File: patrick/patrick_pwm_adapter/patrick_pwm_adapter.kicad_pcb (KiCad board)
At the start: 2 copper layers, 5 parts, among them J1 Conn_01x13, J2 Conn_01x14, U1 TLC5951DAP

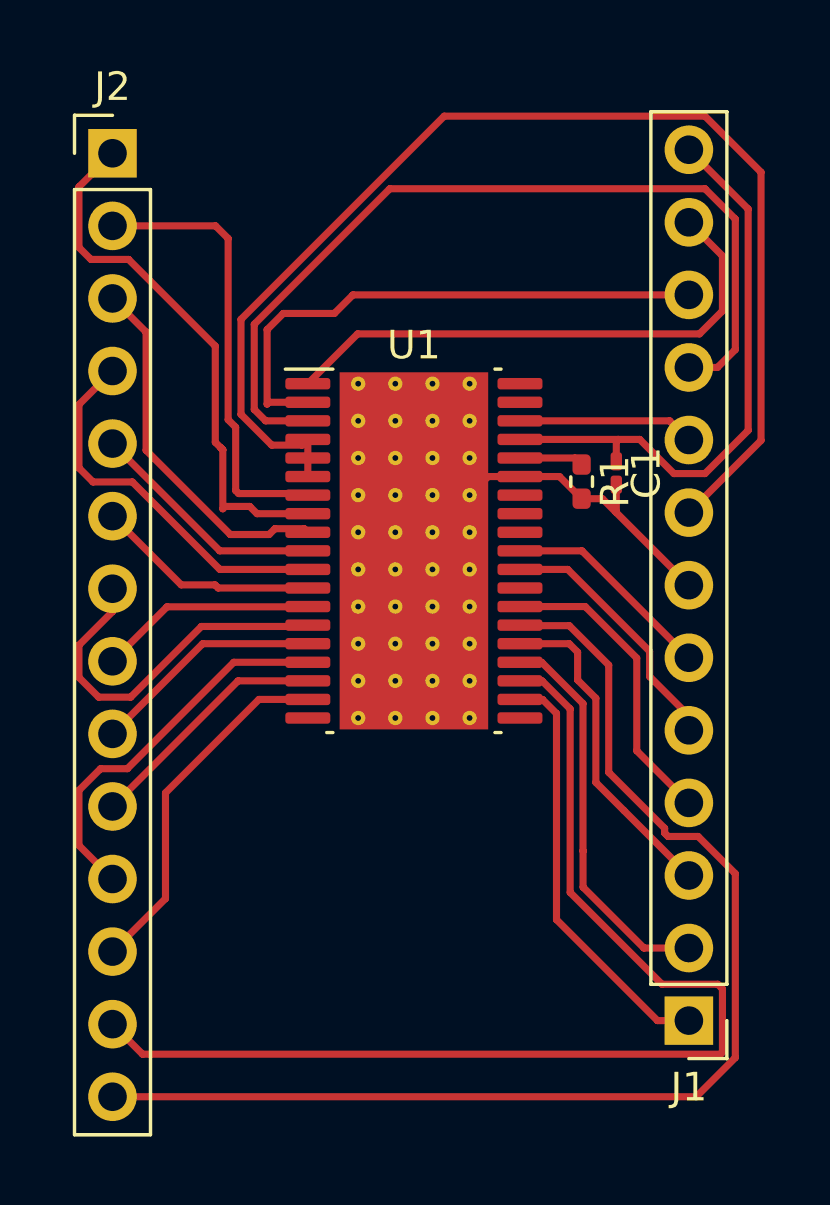
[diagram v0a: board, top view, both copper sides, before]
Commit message: added pwm breakouts
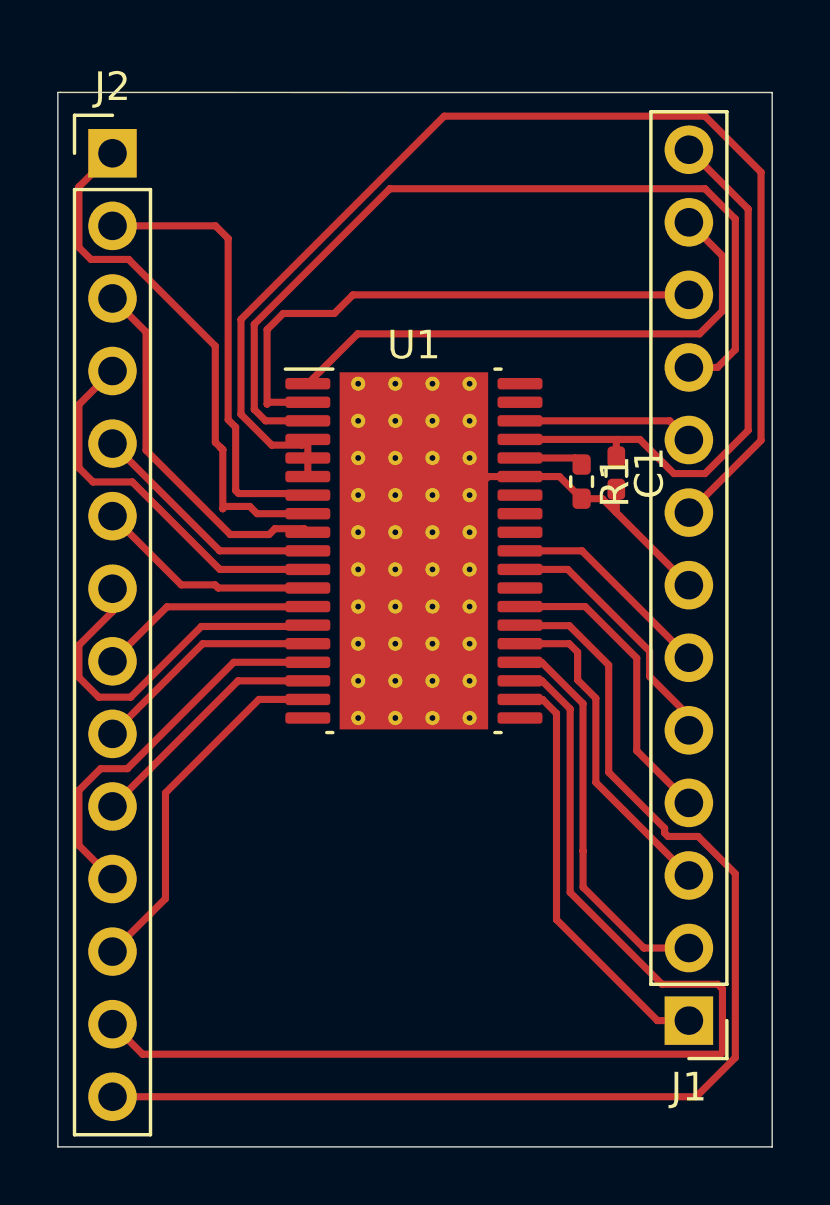
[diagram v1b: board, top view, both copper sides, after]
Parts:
- C1: footprint Capacitor_SMD:C_0201_0603Metric_Pad0.64x0.40mm_HandSolder -> Capacitor_SMD:C_0402_1005Metric_Pad0.74x0.62mm_HandSolder
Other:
- board outline added: 25 x 36.9 mm
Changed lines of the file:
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@@
   (general
     (thickness 1.6)
-    (drawings 0)
+    (drawings 5)
     (tracks 173)
     (zones 0)
@@
     (add_net "Net-(U1-Pad38)")
   )
+  (module Capacitor_SMD:C_0402_1005Metric_Pad0.74x0.62mm_HandSolder (layer F.Cu)
+    (at 166.05758 51.2456 270)
+    (descr "Capacitor SMD 0402 (1005 Metric), square (rectangular) end terminal, IPC_7351 nominal with elongated pad for handsoldering. (Body size source: IPC-SM-782 page 76, https://www.pcb-3d.com/wordpress/wp-content/uploads/ipc-sm-782a_amendment_1_and_2.pdf), generated with kicad-footprint-generator")
+    (tags "capacitor handsolder")
+    (attr smd)
+    (fp_text reference C1 (at 0 -1.16 90) (layer F.SilkS)
+      (effects (font (size 1 1) (thickness 0.15)))
+    )
+    (fp_text value C (at 0 1.16 90) (layer F.Fab)
+      (effects (font (size 1 1) (thickness 0.15)))
+    )
+    (fp_line (start 1.08 0.46) (end -1.08 0.46) (layer F.CrtYd) (width 0.05))
+    (fp_line (start 1.08 -0.46) (end 1.08 0.46) (layer F.CrtYd) (width 0.05))
+    (fp_line (start -1.08 -0.46) (end 1.08 -0.46) (layer F.CrtYd) (width 0.05))
+    (fp_line (start -1.08 0.46) (end -1.08 -0.46) (layer F.CrtYd) (width 0.05))
+    (fp_line (start -0.115835 0.36) (end 0.115835 0.36) (layer F.SilkS) (width 0.12))
+    (fp_line (start -0.115835 -0.36) (end 0.115835 -0.36) (layer F.SilkS) (width 0.12))
+    (fp_line (start 0.5 0.25) (end -0.5 0.25) (layer F.Fab) (width 0.1))
+    (fp_line (start 0.5 -0.25) (end 0.5 0.25) (layer F.Fab) (width 0.1))
+    (fp_line (start -0.5 -0.25) (end 0.5 -0.25) (layer F.Fab) (width 0.1))
+    (fp_line (start -0.5 0.25) (end -0.5 -0.25) (layer F.Fab) (width 0.1))
+    (fp_text user %R (at 0 0 90) (layer F.Fab)
+      (effects (font (size 0.25 0.25) (thickness 0.04)))
+    )
+    (pad 2 smd roundrect (at 0.5675 0 270) (size 0.735 0.62) (layers F.Cu F.Paste F.Mask) (roundrect_rratio 0.25)
+      (net 10 /GND))
+    (pad 1 smd roundrect (at -0.5675 0 270) (size 0.735 0.62) (layers F.Cu F.Paste F.Mask) (roundrect_rratio 0.25)
+      (net 11 /VCC))
+    (model ${KISYS3DMOD}/Capacitor_SMD.3dshapes/C_0402_1005Metric.wrl
+      (at (xyz 0 0 0))
+      (scale (xyz 1 1 1))
+      (rotate (xyz 0 0 0))
+    )
+  )
   (module Resistor_SMD:R_0402_1005Metric_Pad0.72x0.64mm_HandSolder (layer F.Cu)
     (at 164.84346 51.54736 270)
@@
     (fp_text value R_Small_US (at 0 1.17 90) (layer F.Fab)
       (effects (font (size 1 1) (thickness 0.15)))
-    )
-    (fp_text user %R (at 0 0 90) (layer F.Fab)
-      (effects (font (size 0.26 0.26) (thickness 0.04)))
     )
     (fp_line (start -0.525 0.27) (end -0.525 -0.27) (layer F.Fab) (width 0.1))
@@
     (fp_line (start 1.1 -0.47) (end 1.1 0.47) (layer F.CrtYd) (width 0.05))
     (fp_line (start 1.1 0.47) (end -1.1 0.47) (layer F.CrtYd) (width 0.05))
+    (fp_text user %R (at 0 0 90) (layer F.Fab)
+      (effects (font (size 0.26 0.26) (thickness 0.04)))
+    )
     (pad 2 smd roundrect (at 0.5975 0 270) (size 0.715 0.64) (layers F.Cu F.Paste F.Mask) (roundrect_rratio 0.25)
       (net 10 /GND))
@@
     )
     (fp_text value TLC5951DAP (at 0 7.2) (layer F.Fab)
-      (effects (font (size 1 1) (thickness 0.15)))
-    )
-    (fp_text user %R (at 0 0) (layer F.Fab)
       (effects (font (size 1 1) (thickness 0.15)))
     )
@@
     (fp_line (start 4.75 6.5) (end 4.75 -6.5) (layer F.CrtYd) (width 0.05))
     (fp_line (start 4.75 -6.5) (end -4.75 -6.5) (layer F.CrtYd) (width 0.05))
+    (fp_text user %R (at 0 0) (layer F.Fab)
+      (effects (font (size 1 1) (thickness 0.15)))
+    )
     (pad "" smd roundrect (at 0.85 2.12) (size 1.37 1.71) (layers F.Paste) (roundrect_rratio 0.182482))
     (pad "" smd roundrect (at 0.85 0) (size 1.37 1.71) (layers F.Paste) (roundrect_rratio 0.182482))
@@
       (effects (font (size 1 1) (thickness 0.15)))
     )
-    (fp_text user %R (at 0 16.51 90) (layer F.Fab)
-      (effects (font (size 1 1) (thickness 0.15)))
-    )
     (fp_line (start -0.635 -1.27) (end 1.27 -1.27) (layer F.Fab) (width 0.1))
     (fp_line (start 1.27 -1.27) (end 1.27 34.29) (layer F.Fab) (width 0.1))
@@
     (fp_line (start 1.8 34.8) (end 1.8 -1.8) (layer F.CrtYd) (width 0.05))
     (fp_line (start 1.8 -1.8) (end -1.8 -1.8) (layer F.CrtYd) (width 0.05))
+    (fp_text user %R (at 0 16.51 90) (layer F.Fab)
+      (effects (font (size 1 1) (thickness 0.15)))
+    )
     (pad 14 thru_hole oval (at 0 33.02) (size 1.7 1.7) (drill 1) (layers *.Cu *.Mask)
       (net 21 /OUT16))
@@
       (effects (font (size 1 1) (thickness 0.15)))
     )
-    (fp_text user %R (at 0 15.24 90) (layer F.Fab)
-      (effects (font (size 1 1) (thickness 0.15)))
-    )
     (fp_line (start -0.635 -1.27) (end 1.27 -1.27) (layer F.Fab) (width 0.1))
     (fp_line (start 1.27 -1.27) (end 1.27 31.75) (layer F.Fab) (width 0.1))
@@
     (fp_line (start 1.8 32.25) (end 1.8 -1.8) (layer F.CrtYd) (width 0.05))
     (fp_line (start 1.8 -1.8) (end -1.8 -1.8) (layer F.CrtYd) (width 0.05))
+    (fp_text user %R (at 0 15.24 90) (layer F.Fab)
+      (effects (font (size 1 1) (thickness 0.15)))
+    )
     (pad 13 thru_hole oval (at 0 30.48 180) (size 1.7 1.7) (drill 1) (layers *.Cu *.Mask)
       (net 11 /VCC))
@@
     )
   )
-  (module Capacitor_SMD:C_0201_0603Metric_Pad0.64x0.40mm_HandSolder (layer F.Cu)
-    (at 166.05758 51.2456 270)
-    (descr "Capacitor SMD 0201 (0603 Metric), square (rectangular) end terminal, IPC_7351 nominal with elongated pad for handsoldering. (Body size source: https://www.vishay.com/docs/20052/crcw0201e3.pdf), generated with kicad-footprint-generator")
-    (tags "capacitor handsolder")
-    (attr smd)
-    (fp_text reference C1 (at 0 -1.05 90) (layer F.SilkS)
-      (effects (font (size 1 1) (thickness 0.15)))
-    )
-    (fp_text value C (at 0 1.05 90) (layer F.Fab)
-      (effects (font (size 1 1) (thickness 0.15)))
-    )
-    (fp_text user %R (at 0 -0.68 90) (layer F.Fab)
-      (effects (font (size 0.25 0.25) (thickness 0.04)))
-    )
-    (fp_line (start -0.3 0.15) (end -0.3 -0.15) (layer F.Fab) (width 0.1))
-    (fp_line (start -0.3 -0.15) (end 0.3 -0.15) (layer F.Fab) (width 0.1))
-    (fp_line (start 0.3 -0.15) (end 0.3 0.15) (layer F.Fab) (width 0.1))
-    (fp_line (start 0.3 0.15) (end -0.3 0.15) (layer F.Fab) (width 0.1))
-    (fp_line (start -0.88 0.35) (end -0.88 -0.35) (layer F.CrtYd) (width 0.05))
-    (fp_line (start -0.88 -0.35) (end 0.88 -0.35) (layer F.CrtYd) (width 0.05))
-    (fp_line (start 0.88 -0.35) (end 0.88 0.35) (layer F.CrtYd) (width 0.05))
-    (fp_line (start 0.88 0.35) (end -0.88 0.35) (layer F.CrtYd) (width 0.05))
-    (pad 2 smd roundrect (at 0.4075 0 270) (size 0.635 0.4) (layers F.Cu F.Mask) (roundrect_rratio 0.25)
-      (net 10 /GND))
-    (pad 1 smd roundrect (at -0.4075 0 270) (size 0.635 0.4) (layers F.Cu F.Mask) (roundrect_rratio 0.25)
-      (net 11 /VCC))
-    (pad "" smd roundrect (at 0.4325 0 270) (size 0.458 0.36) (layers F.Paste) (roundrect_rratio 0.25))
-    (pad "" smd roundrect (at -0.4325 0 270) (size 0.458 0.36) (layers F.Paste) (roundrect_rratio 0.25))
-    (model ${KISYS3DMOD}/Capacitor_SMD.3dshapes/C_0201_0603Metric.wrl
-      (at (xyz 0 0 0))
-      (scale (xyz 1 1 1))
-      (rotate (xyz 0 0 0))
-    )
-  )
+  (gr_line (start 146.51228 37.92474) (end 146.5961 37.92474) (layer Edge.Cuts) (width 0.05))
+  (gr_line (start 146.51228 74.83094) (end 146.51228 37.92474) (layer Edge.Cuts) (width 0.05))
+  (gr_line (start 171.5135 74.83094) (end 146.51228 74.83094) (layer Edge.Cuts) (width 0.05))
+  (gr_line (start 171.5135 37.92982) (end 171.5135 74.83094) (layer Edge.Cuts) (width 0.05))
+  (gr_line (start 146.5961 37.92474) (end 171.5135 37.92982) (layer Edge.Cuts) (width 0.05))
   (segment (start 164.61352 50.71992) (end 164.84346 50.94986) (width 0.25) (layer F.Cu) (net 1))
   (segment (start 162.68602 50.71992) (end 164.61352 50.71992) (width 0.25) (layer F.Cu) (net 1))
